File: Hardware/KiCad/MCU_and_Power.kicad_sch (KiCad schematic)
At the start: 30 parts

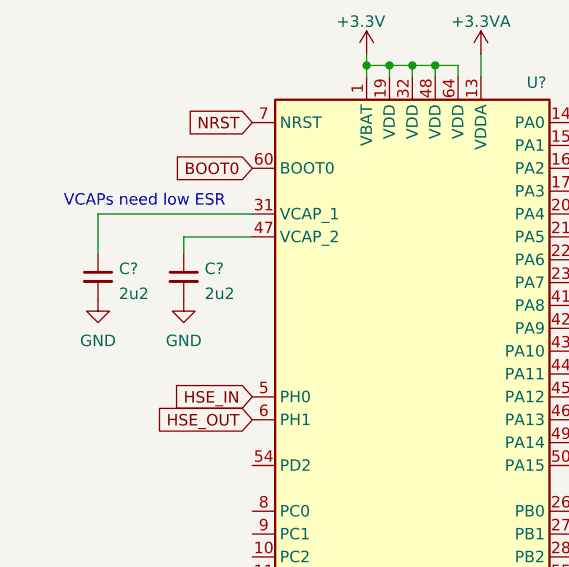
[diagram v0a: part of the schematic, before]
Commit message: added the bmp388 pressure sensor
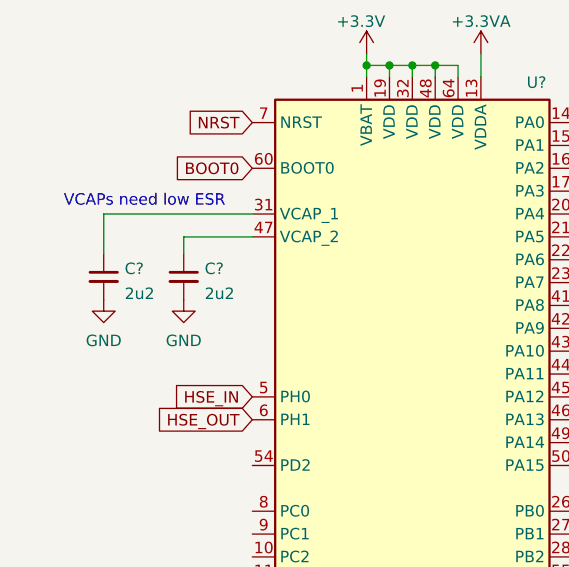
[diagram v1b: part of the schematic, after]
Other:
- moved on the sheet: C?
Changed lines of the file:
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@@
     (stroke (width 0) (type default) (color 0 0 0 0))
   )
-  (wire (pts (xy 27.94 106.045) (xy 27.94 110.49))
+  (wire (pts (xy 28.575 106.045) (xy 28.575 110.49))
     (stroke (width 0) (type default) (color 0 0 0 0))
   )
@@
     (stroke (width 0) (type default) (color 0 0 0 0))
   )
-  (wire (pts (xy 45.085 106.045) (xy 27.94 106.045))
+  (wire (pts (xy 45.085 106.045) (xy 28.575 106.045))
     (stroke (width 0) (type default) (color 0 0 0 0))
   )
@@
     (pin "1")
   )
-  (symbol (lib_id "Device:C_Small") (at 27.94 113.03 0) (unit 1)
-    (in_bom yes) (on_board yes) (fields_autoplaced)
-    (property "Reference" "C?" (id 0) (at 30.2641 112.1278 0)
-      (effects (font (size 1.27 1.27)) (justify left))
-    )
-    (property "Value" "2u2" (id 1) (at 30.2641 114.9029 0)
-      (effects (font (size 1.27 1.27)) (justify left))
-    )
-    (property "Footprint" "" (id 2) (at 27.94 113.03 0)
-      (effects (font (size 1.27 1.27)) hide)
-    )
-    (property "Datasheet" "~" (id 3) (at 27.94 113.03 0)
+  (symbol (lib_id "Device:C_Small") (at 28.575 113.03 0) (unit 1)
+    (in_bom yes) (on_board yes) (fields_autoplaced)
+    (property "Reference" "C?" (id 0) (at 30.8991 112.1278 0)
+      (effects (font (size 1.27 1.27)) (justify left))
+    )
+    (property "Value" "2u2" (id 1) (at 30.8991 114.9029 0)
+      (effects (font (size 1.27 1.27)) (justify left))
+    )
+    (property "Footprint" "" (id 2) (at 28.575 113.03 0)
+      (effects (font (size 1.27 1.27)) hide)
+    )
+    (property "Datasheet" "~" (id 3) (at 28.575 113.03 0)
       (effects (font (size 1.27 1.27)) hide)
     )
@@
     (pin "1")
   )
-  (symbol (lib_id "power:GND") (at 27.94 115.57 0) (unit 1)
-    (in_bom yes) (on_board yes) (fields_autoplaced)
-    (property "Reference" "#PWR0108" (id 0) (at 27.94 121.92 0)
-      (effects (font (size 1.27 1.27)) hide)
-    )
-    (property "Value" "GND" (id 1) (at 27.94 120.1325 0))
-    (property "Footprint" "" (id 2) (at 27.94 115.57 0)
-      (effects (font (size 1.27 1.27)) hide)
-    )
-    (property "Datasheet" "" (id 3) (at 27.94 115.57 0)
-      (effects (font (size 1.27 1.27)) hide)
-    )
+  (symbol (lib_id "power:GND") (at 28.575 115.57 0) (unit 1)
+    (in_bom yes) (on_board yes) (fields_autoplaced)
+    (property "Reference" "#PWR0108" (id 0) (at 28.575 121.92 0)
+      (effects (font (size 1.27 1.27)) hide)
+    )
+    (property "Value" "GND" (id 1) (at 28.575 120.1325 0))
+    (property "Footprint" "" (id 2) (at 28.575 115.57 0)
+      (effects (font (size 1.27 1.27)) hide)
+    )
+    (property "Datasheet" "" (id 3) (at 28.575 115.57 0)
+      (effects (font (size 1.27 1.27)) hide)
+    )

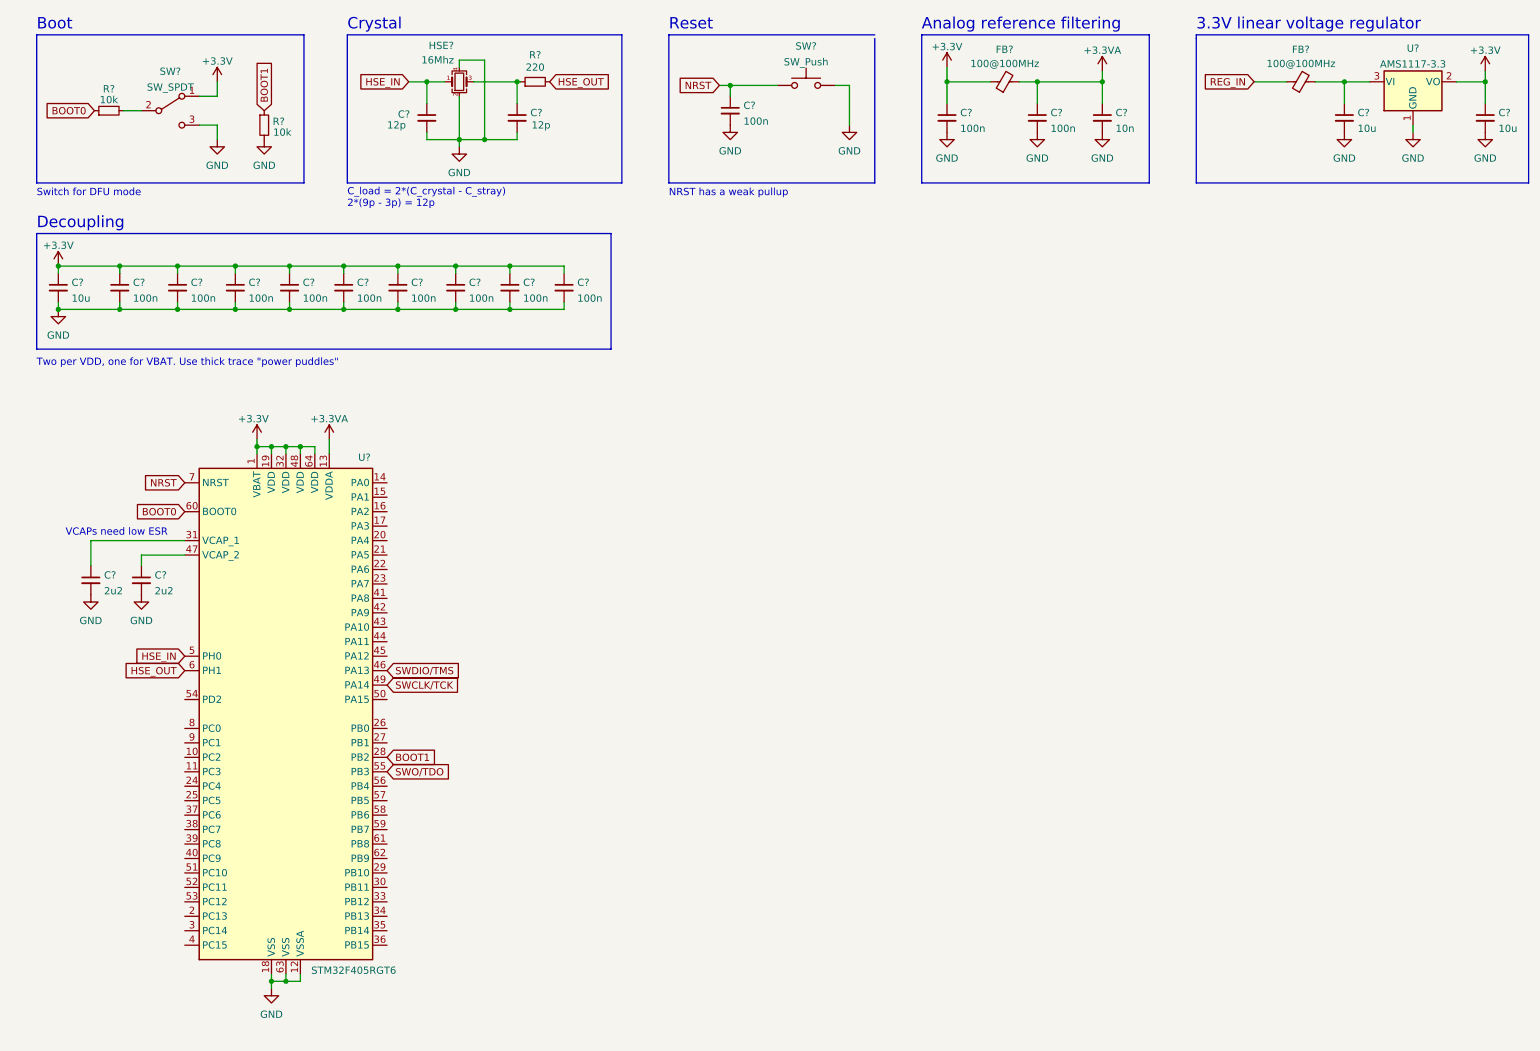
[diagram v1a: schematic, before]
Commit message: changed MCU to STM32H743VIT6
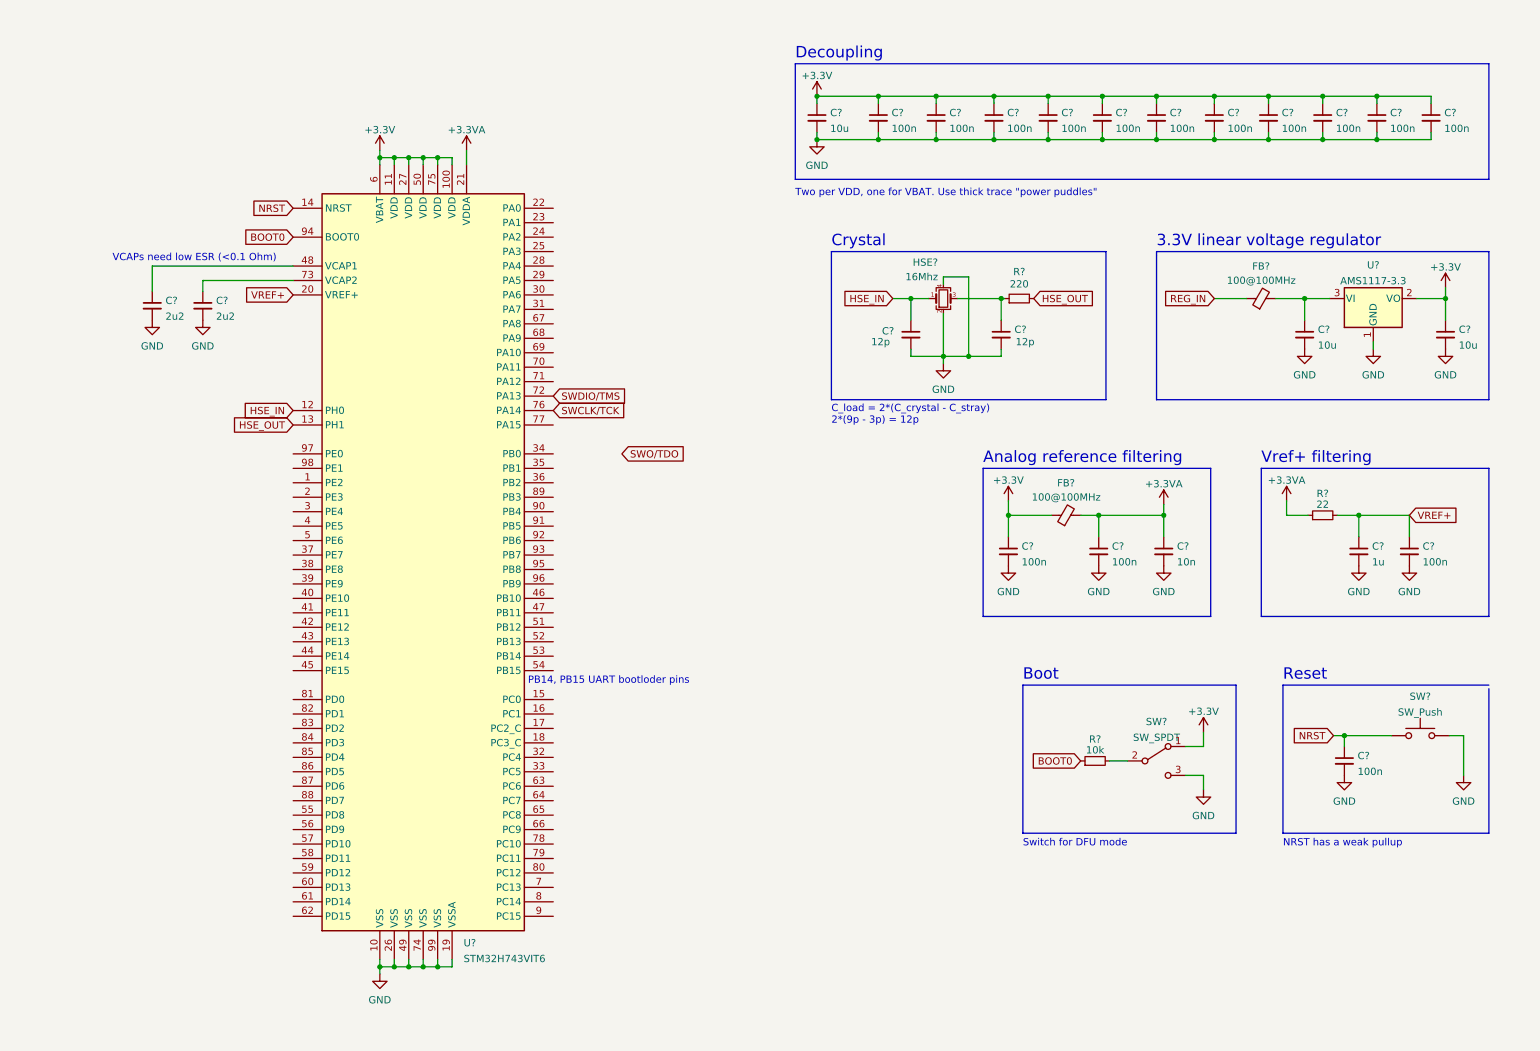
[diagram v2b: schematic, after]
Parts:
- removed C? (x2): 2u2, symbol Device:C_Small
- removed R?: 10k, symbol Device:R_Small
- removed U?: STM32F405RGT6, Package_QFP:LQFP-64_10x10mm_P0.5mm, symbol MCU_ST_STM32F4:STM32F405RGTx
- added C? (x3): 100n, symbol Device:C_Small
- added C?: 1u, symbol Device:C_Small
- added C? (x2): 2u2, symbol Device:C_Small
- added R?: 22, symbol Device:R_Small
- added U?: STM32H743VIT6, Package_QFP:LQFP-100_14x14mm_P0.5mm, symbol MCU_ST_STM32H7:STM32H743VITx
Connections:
- net +3.3VA: now also R?.1, U?.21 (VDDA)
- net +3V3: now also C?.1, C?.1, U?.100 (VDD), U?.11 (VDD), U?.27 (VDD), U?.50 (VDD), U?.6 (VBAT), U?.75 (VDD)
- net BOOT0: now also U?.94 (BOOT0)
- net GND: now also C?.2, C?.2, C?.2, C?.2, C?.2, C?.2, U?.10 (VSS), U?.19 (VSSA), U?.26 (VSS), U?.49 (VSS), U?.74 (VSS), U?.99 (VSS)
- net HSE_IN: now also U?.12 (PH0)
- net HSE_OUT: now also U?.13 (PH1)
- net NRST: now also U?.14 (NRST)
- net SWCLK/TCK: now also U?.76 (PA14)
- net SWDIO/TMS: now also U?.72 (PA13)
- new net: C?.1, U?.48 (VCAP1)
- new net: C?.1, U?.73 (VCAP2)
- new net VREF+: C?.1, C?.1, R?.2, U?.20 (VREF+)
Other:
- note added: "PB14, PB15 UART bootloder pins"
- note added: "VCAPs need low ESR (<0.1 Ohm)"
- note added: "Vref+ filtering"
- note removed: "VCAPs need low ESR"
- moved on the sheet: C?, FB?, HSE?, R?, SW?, U?
